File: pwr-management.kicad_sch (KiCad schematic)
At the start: 22 parts, among them IC2 BQ25176JDSGR, Q1 NMOS, Q2 NMOS, U3 BQ297xy, U4 MCP1640Bx-xCHY, U6 MCP1727-0802xSN

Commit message: set initial component footprints
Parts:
- C1: renamed from C18; footprint (none) -> Capacitor_SMD:C_0603_1608Metric
- C2: renamed from C17; footprint (none) -> Capacitor_SMD:C_0603_1608Metric
- C3: renamed from C19; footprint (none) -> Capacitor_SMD:C_0603_1608Metric
- C4: renamed from C20; footprint (none) -> Capacitor_SMD:C_0603_1608Metric
- IC1: renamed from IC2; footprint SON50P200X200X80-9N -> (none)
- R10: renamed from R21; footprint (none) -> Resistor_SMD:R_0603_1608Metric
- R3: renamed from R8; footprint (none) -> Resistor_SMD:R_0603_1608Metric
- R4: renamed from R16; footprint (none) -> Resistor_SMD:R_0603_1608Metric
- R5: renamed from R18; footprint (none) -> Resistor_SMD:R_0603_1608Metric
- R6: renamed from R19; footprint (none) -> Resistor_SMD:R_0603_1608Metric
- R7: renamed from R9; footprint (none) -> Resistor_SMD:R_0603_1608Metric
- R8: renamed from R17; footprint (none) -> Resistor_SMD:R_0603_1608Metric
- R9: renamed from R20; footprint (none) -> Resistor_SMD:R_0603_1608Metric
- renumbered D5 to D2, D6 to D3, L5 to L1, U3 to U1, U4 to U2, U6 to U3
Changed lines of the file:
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@@
 		(on_board yes)
 		(dnp no)
-		(property "Reference" "IC2"
+		(property "Reference" "IC1"
 			(at 87.63 104.394 0)
 			(effects
@@
 			)
 		)
-		(property "Footprint" "SON50P200X200X80-9N"
+		(property "Footprint" ""
 			(at 99.06 205.41 0)
 			(effects
@@
 			(project ""
 				(path "/3130e1f2-bde1-4b12-bd54-0e1e50bd36da/ab6e6673-c97f-4978-8f9b-ae71c723cdfa"
-					(reference "IC2")
+					(reference "IC1")
 					(unit 1)
 				)
@@
 		(dnp no)
 		(fields_autoplaced yes)
-		(property "Reference" "R8"
+		(property "Reference" "R3"
 			(at 55.88 44.4499 0)
 			(effects
@@
 			)
 		)
-		(property "Footprint" ""
+		(property "Footprint" "Resistor_SMD:R_0603_1608Metric"
 			(at 51.562 45.72 90)
 			(effects
@@
 			(project ""
 				(path "/3130e1f2-bde1-4b12-bd54-0e1e50bd36da/ab6e6673-c97f-4978-8f9b-ae71c723cdfa"
-					(reference "R8")
+					(reference "R3")
 					(unit 1)
 				)
@@
 		(on_board yes)
 		(dnp no)
-		(property "Reference" "#PWR030"
+		(property "Reference" "#PWR05"
 			(at 87.63 152.4 0)
 			(effects
@@
 			(project "pipu-zero"
 				(path "/3130e1f2-bde1-4b12-bd54-0e1e50bd36da/ab6e6673-c97f-4978-8f9b-ae71c723cdfa"
-					(reference "#PWR030")
+					(reference "#PWR05")
 					(unit 1)
 				)
@@
 		(dnp no)
 		(fields_autoplaced yes)
-		(property "Reference" "C18"
+		(property "Reference" "C1"
 			(at 40.64 121.9262 0)
 			(effects
@@
 			)
 		)
-		(property "Footprint" ""
+		(property "Footprint" "Capacitor_SMD:C_0603_1608Metric"
 			(at 38.1 123.19 0)
 			(effects
@@
 			(project ""
 				(path "/3130e1f2-bde1-4b12-bd54-0e1e50bd36da/ab6e6673-c97f-4978-8f9b-ae71c723cdfa"
-					(reference "C18")
+					(reference "C1")
 					(unit 1)
 				)
@@
 		(on_board yes)
 		(dnp no)
-		(property "Reference" "#PWR039"
+		(property "Reference" "#PWR07"
 			(at 185.42 76.2 0)
 			(effects
@@
 			(project "pipu-zero"
 				(path "/3130e1f2-bde1-4b12-bd54-0e1e50bd36da/ab6e6673-c97f-4978-8f9b-ae71c723cdfa"
-					(reference "#PWR039")
+					(reference "#PWR07")
 					(unit 1)
 				)
@@
 		(dnp no)
 		(fields_autoplaced yes)
-		(property "Reference" "C17"
+		(property "Reference" "C2"
 			(at 57.15 64.7699 0)
 			(effects
@@
 			)
 		)
-		(property "Footprint" ""
+		(property "Footprint" "Capacitor_SMD:C_0603_1608Metric"
 			(at 54.3052 69.85 0)
 			(effects
@@
 			(project ""
 				(path "/3130e1f2-bde1-4b12-bd54-0e1e50bd36da/ab6e6673-c97f-4978-8f9b-ae71c723cdfa"
-					(reference "C17")
+					(reference "C2")
 					(unit 1)
 				)
@@
 		(dnp no)
 		(fields_autoplaced yes)
-		(property "Reference" "R9"
+		(property "Reference" "R7"
 			(at 118.11 72.3899 0)
 			(effects
@@
 			)
 		)
-		(property "Footprint" ""
+		(property "Footprint" "Resistor_SMD:R_0603_1608Metric"
 			(at 113.792 73.66 90)
 			(effects
@@
 			(project ""
 				(path "/3130e1f2-bde1-4b12-bd54-0e1e50bd36da/ab6e6673-c97f-4978-8f9b-ae71c723cdfa"
-					(reference "R9")
+					(reference "R7")
 					(unit 1)
 				)
@@
 		(dnp no)
 		(fields_autoplaced yes)
-		(property "Reference" "D5"
+		(property "Reference" "D2"
 			(at 106.68 124.1424 90)
 			(effects
@@
 			(project ""
 				(path "/3130e1f2-bde1-4b12-bd54-0e1e50bd36da/ab6e6673-c97f-4978-8f9b-ae71c723cdfa"
-					(reference "D5")
+					(reference "D2")
 					(unit 1)
 				)
@@
 		(on_board yes)
 		(dnp no)
-		(property "Reference" "R21"
+		(property "Reference" "R10"
 			(at 187.198 67.31 90)
 			(effects
@@
 			)
 		)
-		(property "Footprint" ""
+		(property "Footprint" "Resistor_SMD:R_0603_1608Metric"
 			(at 185.42 66.04 0)
 			(effects
@@
 			(project "pipu-zero"
 				(path "/3130e1f2-bde1-4b12-bd54-0e1e50bd36da/ab6e6673-c97f-4978-8f9b-ae71c723cdfa"
-					(reference "R21")
+					(reference "R10")
 					(unit 1)
 				)
@@
 		(dnp no)
 		(fields_autoplaced yes)
-		(property "Reference" "U3"
+		(property "Reference" "U1"
 			(at 76.2 46.99 0)
 			(effects
@@
 			(project "pipu-zero"
 				(path "/3130e1f2-bde1-4b12-bd54-0e1e50bd36da/ab6e6673-c97f-4978-8f9b-ae71c723cdfa"
-					(reference "U3")
+					(reference "U1")
 					(unit 1)
 				)
@@
 		(dnp no)
 		(fields_autoplaced yes)
-		(property "Reference" "L5"
+		(property "Reference" "L1"
 			(at 171.45 39.37 90)
 			(effects
@@
 			(project ""
 				(path "/3130e1f2-bde1-4b12-bd54-0e1e50bd36da/ab6e6673-c97f-4978-8f9b-ae71c723cdfa"
-					(reference "L5")
+					(reference "L1")
 					(unit 1)
 				)
@@
 		(dnp no)
 		(fields_autoplaced yes)
-		(property "Reference" "C19"
+		(property "Reference" "C3"
 			(at 135.89 111.7662 0)
 			(effects
@@
 			)
 		)
-		(property "Footprint" ""
+		(property "Footprint" "Capacitor_SMD:C_0603_1608Metric"
 			(at 133.35 113.03 0)
 			(effects
@@
 			(project ""
 				(path "/3130e1f2-bde1-4b12-bd54-0e1e50bd36da/ab6e6673-c97f-4978-8f9b-ae71c723cdfa"
-					(reference "C19")
+					(reference "C3")
 					(unit 1)
 				)
@@
 		(dnp no)
 		(fields_autoplaced yes)
-		(property "Reference" "D6"
+		(property "Reference" "D3"
 			(at 115.57 124.1424 90)
 			(effects
@@
 			(project "pipu-zero"
 				(path "/3130e1f2-bde1-4b12-bd54-0e1e50bd36da/ab6e6673-c97f-4978-8f9b-ae71c723cdfa"
-					(reference "D6")
+					(reference "D3")
 					(unit 1)
 				)
@@
 		(dnp no)
 		(fields_autoplaced yes)
-		(property "Reference" "U6"
+		(property "Reference" "U3"
 			(at 233.68 44.45 0)
 			(effects
@@
 			(project ""
 				(path "/3130e1f2-bde1-4b12-bd54-0e1e50bd36da/ab6e6673-c97f-4978-8f9b-ae71c723cdfa"
-					(reference "U6")
+					(reference "U3")
 					(unit 1)
 				)
@@
 		(dnp no)
 		(fields_autoplaced yes)
-		(property "Reference" "R16"
+		(property "Reference" "R4"
 			(at 57.15 120.6499 0)
 			(effects
@@
 			)
 		)
-		(property "Footprint" ""
+		(property "Footprint" "Resistor_SMD:R_0603_1608Metric"
 			(at 54.61 121.92 0)
 			(effects
@@
 			(project ""
 				(path "/3130e1f2-bde1-4b12-bd54-0e1e50bd36da/ab6e6673-c97f-4978-8f9b-ae71c723cdfa"
-					(reference "R16")
+					(reference "R4")
 					(unit 1)
 				)
@@
 		(on_board yes)
 		(dnp no)
-		(property "Reference" "R20"
+		(property "Reference" "R9"
 			(at 187.198 62.484 90)
 			(effects
@@
 			)
 		)
-		(property "Footprint" ""
+		(property "Footprint" "Resistor_SMD:R_0603_1608Metric"
 			(at 185.42 60.96 0)
 			(effects
@@
 			(project ""
 				(path "/3130e1f2-bde1-4b12-bd54-0e1e50bd36da/ab6e6673-c97f-4978-8f9b-ae71c723cdfa"
-					(reference "R20")
+					(reference "R9")
 					(unit 1)
 				)
@@
 		(dnp no)
 		(fields_autoplaced yes)
-		(property "Reference" "R17"
+		(property "Reference" "R8"
 			(at 123.19 121.9199 0)
 			(effects
@@
 			)
 		)
-		(property "Footprint" ""
+		(property "Footprint" "Resistor_SMD:R_0603_1608Metric"
 			(at 120.65 123.19 0)
 			(effects
@@
 			(project "pipu-zero"
 				(path "/3130e1f2-bde1-4b12-bd54-0e1e50bd36da/ab6e6673-c97f-4978-8f9b-ae71c723cdfa"
-					(reference "R17")
+					(reference "R8")
 					(unit 1)
 				)
@@
 		(on_board yes)
 		(dnp no)
-		(property "Reference" "#PWR041"
+		(property "Reference" "#PWR09"
 			(at 233.68 73.66 0)
 			(effects
@@
 			(project "pipu-zero"
 				(path "/3130e1f2-bde1-4b12-bd54-0e1e50bd36da/ab6e6673-c97f-4978-8f9b-ae71c723cdfa"
-					(reference "#PWR041")
+					(reference "#PWR09")
 					(unit 1)
 				)
@@
 		(on_board yes)
 		(dnp no)
-		(property "Reference" "#PWR040"
+		(property "Reference" "#PWR08"
 			(at 219.71 73.66 0)
 			(effects
@@
 			(project ""
 				(path "/3130e1f2-bde1-4b12-bd54-0e1e50bd36da/ab6e6673-c97f-4978-8f9b-ae71c723cdfa"
-					(reference "#PWR040")
+					(reference "#PWR08")
 					(unit 1)
 				)
@@
 		(on_board yes)
 		(dnp no)
-		(property "Reference" "#PWR038"
+		(property "Reference" "#PWR06"
 			(at 171.45 76.2 0)
 			(effects
@@
 			(project ""
 				(path "/3130e1f2-bde1-4b12-bd54-0e1e50bd36da/ab6e6673-c97f-4978-8f9b-ae71c723cdfa"
-					(reference "#PWR038")
+					(reference "#PWR06")
 					(unit 1)
 				)
@@
 		(dnp no)
 		(fields_autoplaced yes)
-		(property "Reference" "R19"
+		(property "Reference" "R6"
 			(at 115.57 134.6199 0)
 			(effects
@@
 			)
 		)
-		(property "Footprint" ""
+		(property "Footprint" "Resistor_SMD:R_0603_1608Metric"
 			(at 113.03 135.89 0)
 			(effects
@@
 			(project "pipu-zero"
 				(path "/3130e1f2-bde1-4b12-bd54-0e1e50bd36da/ab6e6673-c97f-4978-8f9b-ae71c723cdfa"
-					(reference "R19")
+					(reference "R6")
 					(unit 1)
 				)
@@
 		(on_board yes)
 		(dnp no)
-		(property "Reference" "#PWR042"
+		(property "Reference" "#PWR010"
 			(at 260.35 54.61 0)
 			(effects
@@
 			(project ""
 				(path "/3130e1f2-bde1-4b12-bd54-0e1e50bd36da/ab6e6673-c97f-4978-8f9b-ae71c723cdfa"
-					(reference "#PWR042")
+					(reference "#PWR010")
 					(unit 1)
 				)
@@
 		(on_board yes)
 		(dnp no)
-		(property "Reference" "C20"
+		(property "Reference" "C4"
 			(at 213.36 60.706 0)
 			(effects
@@
 			)
 		)
-		(property "Footprint" ""
+		(property "Footprint" "Capacitor_SMD:C_0603_1608Metric"
 			(at 220.6752 66.04 0)
 			(effects
@@
 			(project ""
 				(path "/3130e1f2-bde1-4b12-bd54-0e1e50bd36da/ab6e6673-c97f-4978-8f9b-ae71c723cdfa"
-					(reference "C20")
+					(reference "C4")
 					(unit 1)
 				)
@@
 		(dnp no)
 		(fields_autoplaced yes)
-		(property "Reference" "U4"
+		(property "Reference" "U2"
 			(at 171.45 48.26 0)
 			(effects
@@
 			(project ""
 				(path "/3130e1f2-bde1-4b12-bd54-0e1e50bd36da/ab6e6673-c97f-4978-8f9b-ae71c723cdfa"
-					(reference "U4")
+					(reference "U2")
 					(unit 1)
 				)
@@
 		(dnp no)
 		(fields_autoplaced yes)
-		(property "Reference" "R18"
+		(property "Reference" "R5"
 			(at 106.68 134.6199 0)
 			(effects
@@
 			)
 		)
-		(property "Footprint" ""
+		(property "Footprint" "Resistor_SMD:R_0603_1608Metric"
 			(at 104.14 135.89 0)
 			(effects
@@
 			(project "pipu-zero"
 				(path "/3130e1f2-bde1-4b12-bd54-0e1e50bd36da/ab6e6673-c97f-4978-8f9b-ae71c723cdfa"
-					(reference "R18")
-					(unit 1)
-				)
+					(reference "R5")
+					(unit 1)
+				)

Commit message: Add footprints
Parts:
- BT1: footprint (none) -> Connector_PinSocket_2.54mm:PinSocket_1x02_P2.54mm_Vertical
- D2, D3: footprint (none) -> LED_SMD:LED_0805_2012Metric
- IC1: footprint (none) -> BQ25176J:SON50P200X200X80-9N
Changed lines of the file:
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@@
 			)
 		)
-		(property "Footprint" ""
+		(property "Footprint" "BQ25176J:SON50P200X200X80-9N"
 			(at 99.06 205.41 0)
 			(effects
@@
 			)
 		)
-		(property "Footprint" ""
+		(property "Footprint" "LED_SMD:LED_0805_2012Metric"
 			(at 104.14 127 0)
 			(effects
@@
 			)
 		)
-		(property "Footprint" ""
+		(property "Footprint" "Connector_PinSocket_2.54mm:PinSocket_1x02_P2.54mm_Vertical"
 			(at 33.02 56.896 90)
 			(effects
@@
 			)
 		)
-		(property "Footprint" ""
+		(property "Footprint" "LED_SMD:LED_0805_2012Metric"
 			(at 113.03 127 0)
 			(effects

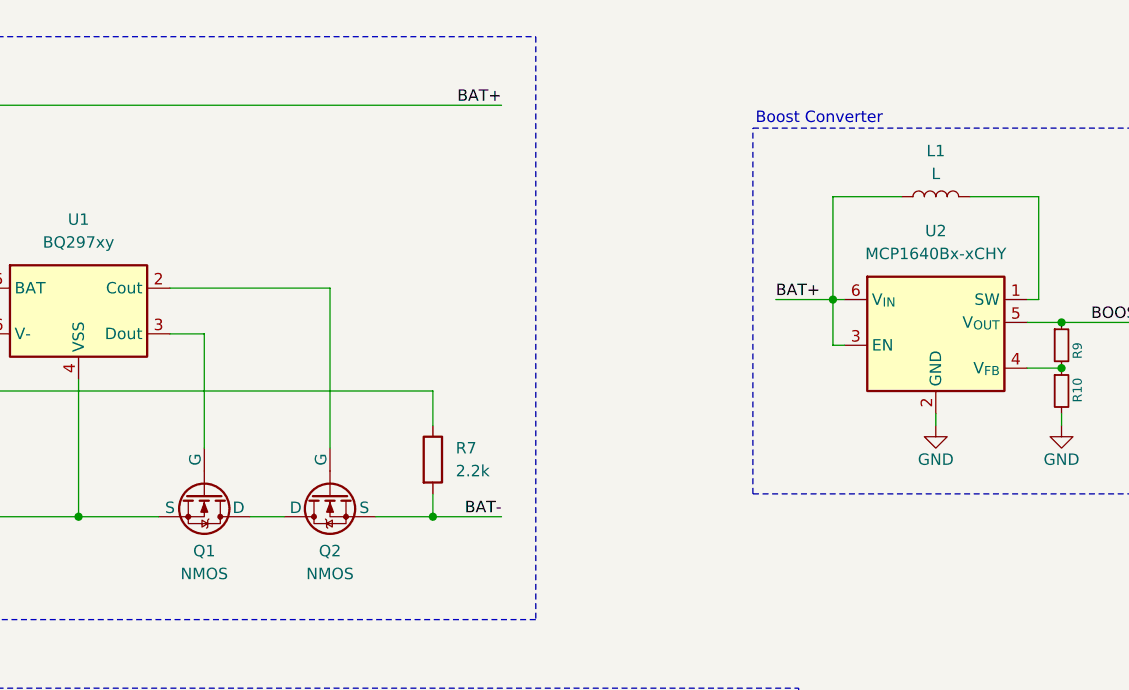
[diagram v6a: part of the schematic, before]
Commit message: Add footprints
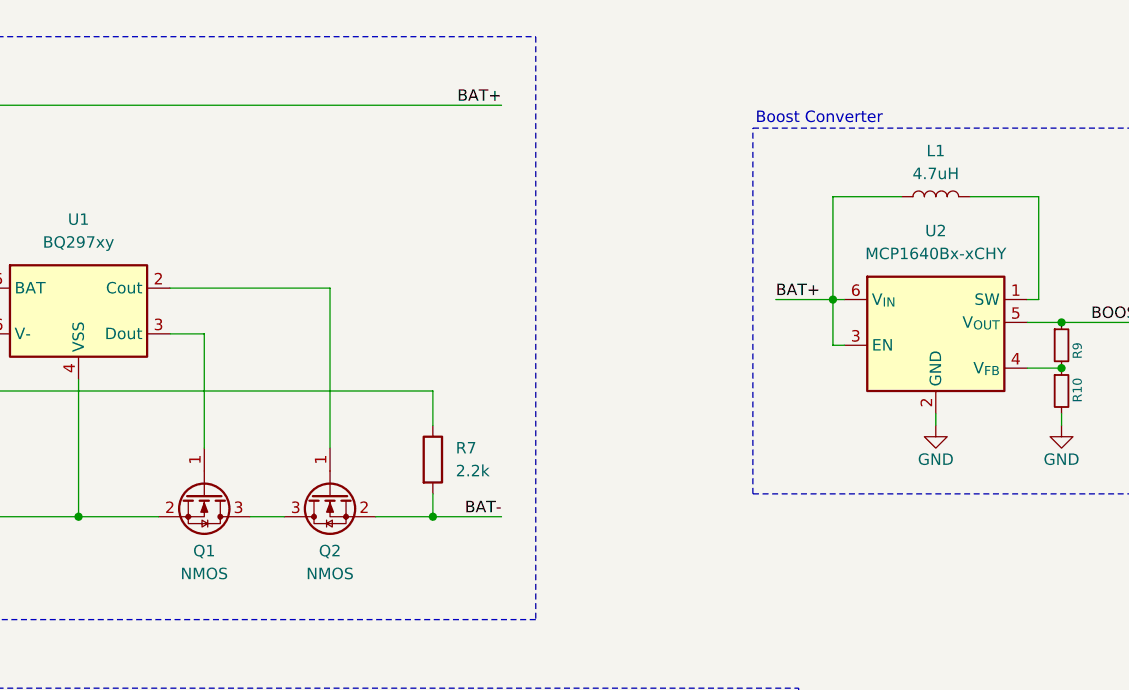
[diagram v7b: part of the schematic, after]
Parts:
- removed Q2: NMOS, symbol Simulation_SPICE:NMOS
- added Q2: NMOS, Package_TO_SOT_SMD:SOT-23, symbol Transistor_FET:Q_NMOS_GSD
- L1: value L -> 4.7uH; footprint (none) -> CPT-9019S-SMT-TR:CPT9019SSMTTR
- Q1: footprint (none) -> Package_TO_SOT_SMD:SOT-23; symbol Simulation_SPICE:NMOS -> Transistor_FET:Q_NMOS_GSD
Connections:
- net GND: now also Q2.2 (S)
- net at BT1.2 (-), C2.2, U1.4 (VSS): now also Q1.2 (S); no longer Q1.3 (S)
- net at U1.2 (Cout): now also Q2.1 (G)
- net at U1.3 (Dout): now also Q1.1 (G); no longer Q1.2 (G)
- new net: Q1.3 (D), Q2.3 (D)
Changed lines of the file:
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@@
 			)
 		)
-		(property "Value" "L"
+		(property "Value" "4.7uH"
 			(at 171.45 41.91 90)
 			(effects
@@
 			)
 		)
-		(property "Footprint" ""
+		(property "Footprint" "CPT-9019S-SMT-TR:CPT9019SSMTTR"
 			(at 171.45 44.45 0)
 			(effects
@@
 	)
 	(symbol
+		(lib_id "Transistor_FET:Q_NMOS_GSD")
+		(at 104.14 77.47 90)
+		(mirror x)
+		(unit 1)
+		(exclude_from_sim no)
+		(in_bom yes)
+		(on_board yes)
+		(dnp no)
+		(property "Reference" "Q2"
+			(at 104.14 83.82 90)
+			(effects
+				(font
+					(size 1.27 1.27)
+				)
+			)
+		)
+		(property "Value" "NMOS"
+			(at 104.14 86.36 90)
+			(effects
+				(font
+					(size 1.27 1.27)
+				)
+			)
+		)
+		(property "Footprint" "Package_TO_SOT_SMD:SOT-23"
+			(at 101.6 82.55 0)
+			(effects
+				(font
+					(size 1.27 1.27)
+				)
+				(hide yes)
+			)
+		)
+		(property "Datasheet" "~"
+			(at 104.14 77.47 0)
+			(effects
+				(font
+					(size 1.27 1.27)
+				)
+				(hide yes)
+			)
+		)
+		(property "Description" "N-MOSFET transistor, gate/source/drain"
+			(at 104.14 77.47 0)
+			(effects
+				(font
+					(size 1.27 1.27)
+				)
+				(hide yes)
+			)
+		)
+		(property "Sim.Device" "NMOS"
+			(at 121.285 77.47 0)
+			(effects
+				(font
+					(size 1.27 1.27)
+				)
+				(hide yes)
+			)
+		)
+		(property "Sim.Type" "VDMOS"
+			(at 123.19 77.47 0)
+			(effects
+				(font
+					(size 1.27 1.27)
+				)
+				(hide yes)
+			)
+		)
+		(property "Sim.Pins" "1=D 2=G 3=S"
+			(at 119.38 77.47 0)
+			(effects
+				(font
+					(size 1.27 1.27)
+				)
+				(hide yes)
+			)
+		)
+		(pin "3"
+		)
+		(pin "1"
+		)
+		(pin "2"
+		)
+		(instances
+			(project "pipu-zero"
+				(path "/3130e1f2-bde1-4b12-bd54-0e1e50bd36da/ab6e6673-c97f-4978-8f9b-ae71c723cdfa"
+					(reference "Q2")
+					(unit 1)
+				)
+			)
+		)
+	)
+	(symbol
 		(lib_id "Device:Battery_Cell")
 		(at 33.02 58.42 0)
@@
 	)
 	(symbol
-		(lib_id "Simulation_SPICE:NMOS")
+		(lib_id "Transistor_FET:Q_NMOS_GSD")
 		(at 90.17 77.47 270)
 		(unit 1)
@@
 			)
 		)
-		(property "Footprint" ""
+		(property "Footprint" "Package_TO_SOT_SMD:SOT-23"
 			(at 92.71 82.55 0)
 			(effects
@@
 			)
 		)
-		(property "Datasheet" "https://ngspice.sourceforge.io/docs/ngspice-html-manual/manual.xhtml#cha_MOSFETs"
-			(at 77.47 77.47 0)
-			(effects
-				(font
-					(size 1.27 1.27)
-				)
-				(hide yes)
-			)
-		)
-		(property "Description" "N-MOSFET transistor, drain/source/gate"
+		(property "Datasheet" "~"
+			(at 90.17 77.47 0)
+			(effects
+				(font
+					(size 1.27 1.27)
+				)
+				(hide yes)
+			)
+		)
+		(property "Description" "N-MOSFET transistor, gate/source/drain"
 			(at 90.17 77.47 0)
 			(effects
@@
 					(unit 1)
 				)
-			)
-		)
-	)
-	(symbol
-		(lib_id "Simulation_SPICE:NMOS")
-		(at 104.14 77.47 90)
-		(mirror x)
-		(unit 1)
-		(exclude_from_sim no)
-		(in_bom yes)
-		(on_board yes)
-		(dnp no)
-		(property "Reference" "Q2"
-			(at 104.14 83.82 90)
-			(effects
-				(font
-					(size 1.27 1.27)
-				)
-			)
-		)
-		(property "Value" "NMOS"
-			(at 104.14 86.36 90)
-			(effects
-				(font
-					(size 1.27 1.27)
-				)
-			)
-		)
-		(property "Footprint" ""
-			(at 101.6 82.55 0)
-			(effects
-				(font
-					(size 1.27 1.27)
-				)
-				(hide yes)
-			)
-		)
-		(property "Datasheet" "https://ngspice.sourceforge.io/docs/ngspice-html-manual/manual.xhtml#cha_MOSFETs"
-			(at 116.84 77.47 0)
-			(effects
-				(font
-					(size 1.27 1.27)
-				)
-				(hide yes)
-			)
-		)
-		(property "Description" "N-MOSFET transistor, drain/source/gate"
-			(at 104.14 77.47 0)
-			(effects
-				(font
-					(size 1.27 1.27)
-				)
-				(hide yes)
-			)
-		)
-		(property "Sim.Device" "NMOS"
-			(at 121.285 77.47 0)
-			(effects
-				(font
-					(size 1.27 1.27)
-				)
-				(hide yes)
-			)
-		)
-		(property "Sim.Type" "VDMOS"
-			(at 123.19 77.47 0)
-			(effects
-				(font
-					(size 1.27 1.27)
-				)
-				(hide yes)
-			)
-		)
-		(property "Sim.Pins" "1=D 2=G 3=S"
-			(at 119.38 77.47 0)
-			(effects
-				(font
-					(size 1.27 1.27)
-				)
-				(hide yes)
-			)
-		)
-		(pin "3"
-		)
-		(pin "1"
-		)
-		(pin "2"
-		)
-		(instances
-			(project "pipu-zero"
-				(path "/3130e1f2-bde1-4b12-bd54-0e1e50bd36da/ab6e6673-c97f-4978-8f9b-ae71c723cdfa"
-					(reference "Q2")
-					(unit 1)
-				)

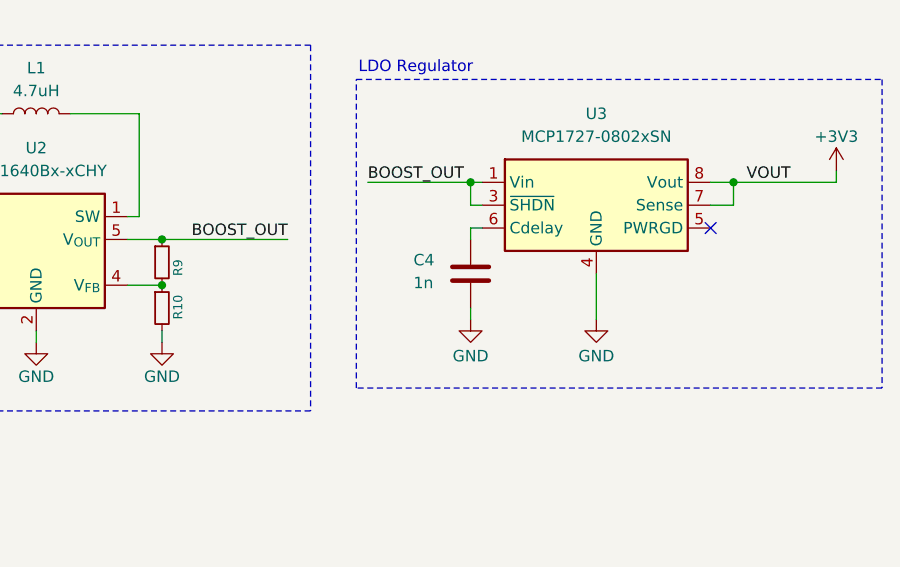
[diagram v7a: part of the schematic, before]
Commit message: Add bypass capacitors
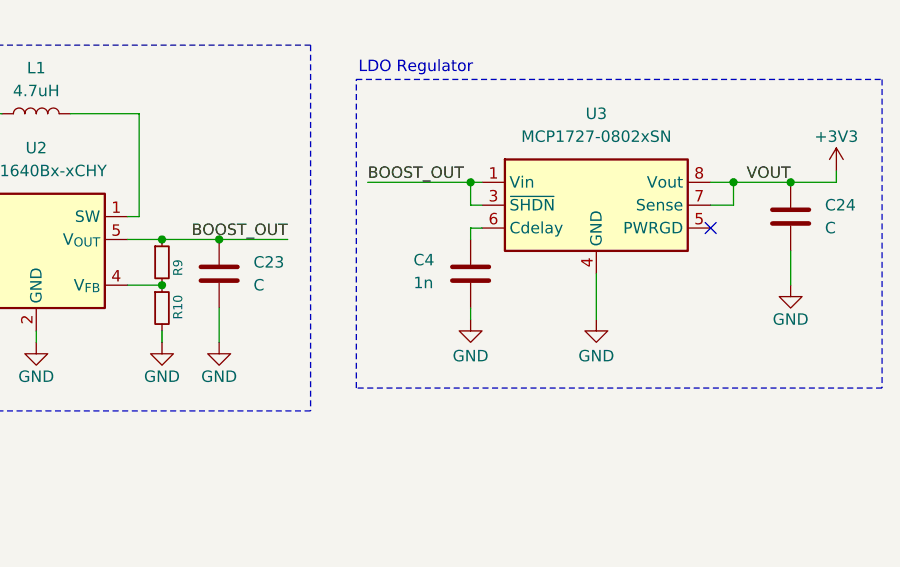
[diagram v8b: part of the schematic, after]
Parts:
- added C23, C24: C, Capacitor_SMD:C_0805_2012Metric, symbol Device:C
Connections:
- net +3V3: now also C24.1
- net BOOST_OUT: now also C23.1
- net GND: now also C23.2, C24.2
